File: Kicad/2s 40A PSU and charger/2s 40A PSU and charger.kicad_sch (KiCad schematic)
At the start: 5 parts

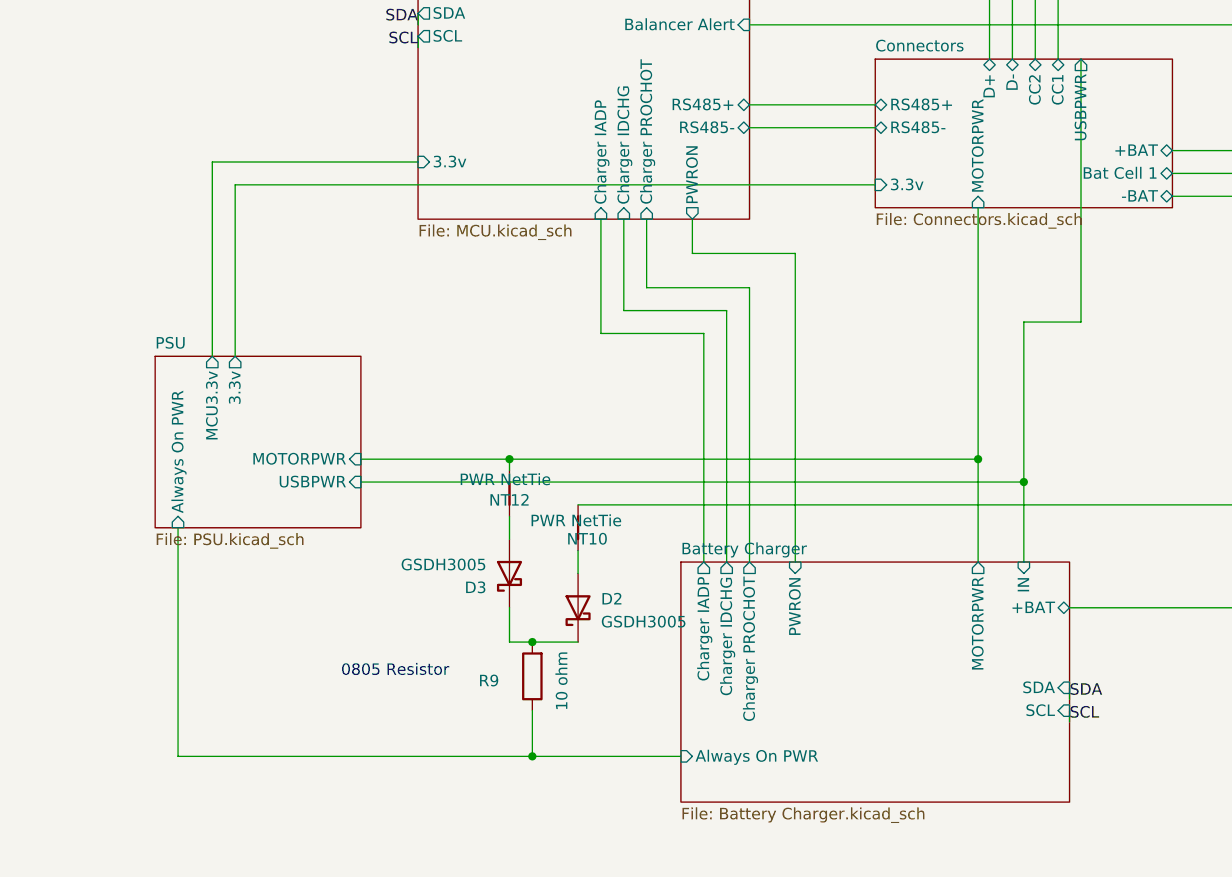
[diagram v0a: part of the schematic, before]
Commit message: Disconnect REGN from unneeded output pullups
These pullups will instead be pulled to 3v3, which should be closer locally. I don't use them but pullups are required for internal detection.
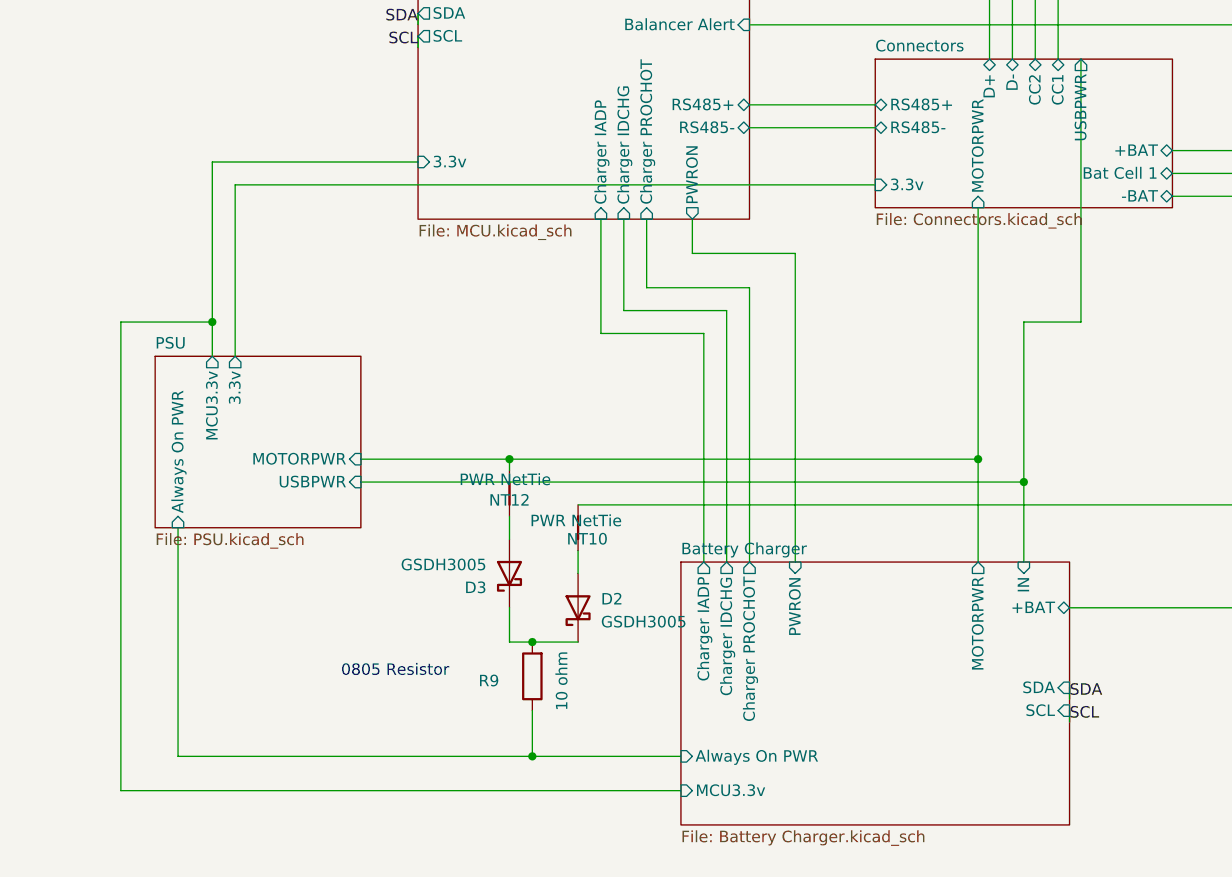
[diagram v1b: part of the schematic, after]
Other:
- sheet Battery Charger ports: added MCU3.3v; removed none
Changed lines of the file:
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@@
+	)
+	(junction
+		(at 74.93 99.06)
+		(diameter 0)
+		(color 0 0 0 0)
 	)
 	(junction
@@
 	(wire
 		(pts
+			(xy 64.77 99.06) (xy 74.93 99.06)
+		)
+		(stroke
+			(width 0)
+			(type default)
+		)
+	)
+	(wire
+		(pts
 			(xy 163.83 59.69) (xy 134.62 59.69)
 		)
@@
 	(wire
 		(pts
+			(xy 74.93 99.06) (xy 74.93 81.28)
+		)
+		(stroke
+			(width 0)
+			(type default)
+		)
+	)
+	(wire
+		(pts
 			(xy 166.37 69.85) (xy 166.37 57.15)
 		)
@@
 	(wire
 		(pts
-			(xy 74.93 102.87) (xy 74.93 81.28)
+			(xy 74.93 102.87) (xy 74.93 99.06)
 		)
 		(stroke
@@
 	(wire
 		(pts
+			(xy 127 151.13) (xy 64.77 151.13)
+		)
+		(stroke
+			(width 0)
+			(type default)
+		)
+	)
+	(wire
+		(pts
 			(xy 110.49 142.24) (xy 110.49 147.32)
 		)
@@
 		(pts
 			(xy 115.57 127) (xy 115.57 124.46)
+		)
+		(stroke
+			(width 0)
+			(type default)
+		)
+	)
+	(wire
+		(pts
+			(xy 64.77 151.13) (xy 64.77 99.06)
 		)
 		(stroke
@@
 	(sheet
 		(at 127 125.73)
-		(size 43.18 26.67)
+		(size 43.18 29.21)
 		(fields_autoplaced yes)
 		(stroke
@@
 		)
 		(property "Sheetfile" "Battery Charger.kicad_sch"
-			(at 127 152.9846 0)
+			(at 127 155.5246 0)
 			(effects
 				(font
@@
 			(effects
 				(font
+					(size 1.27 1.27)
+				)
+				(justify left)
+			)
+		)
+		(pin "MCU3.3v" input
+			(at 127 151.13 180)
+			(effects
+				(font

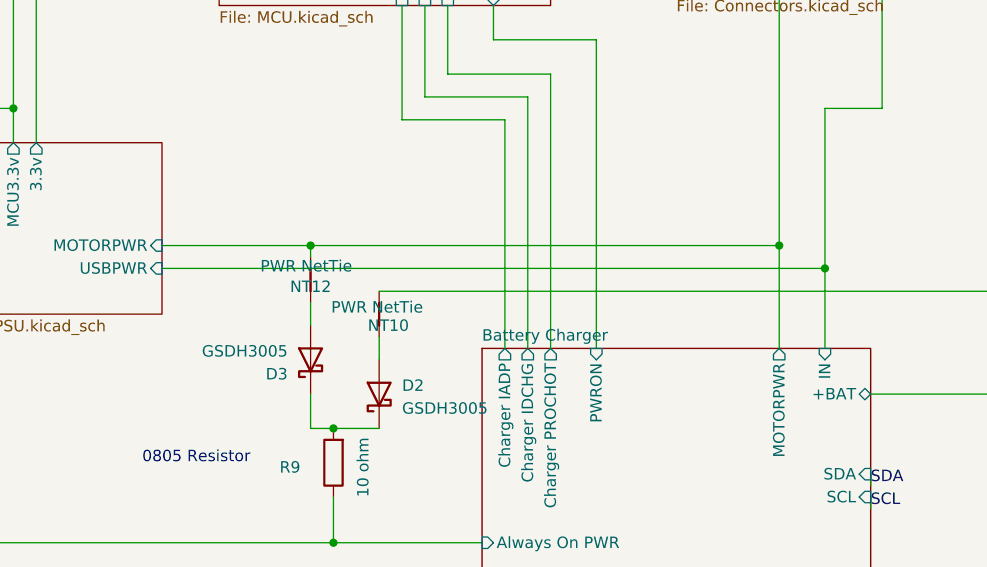
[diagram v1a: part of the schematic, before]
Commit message: Fixed Always On PWR connection
I had it connected to motor power and battery power, what it should have been connected to was USB-C and battery, no barriers whatsoever
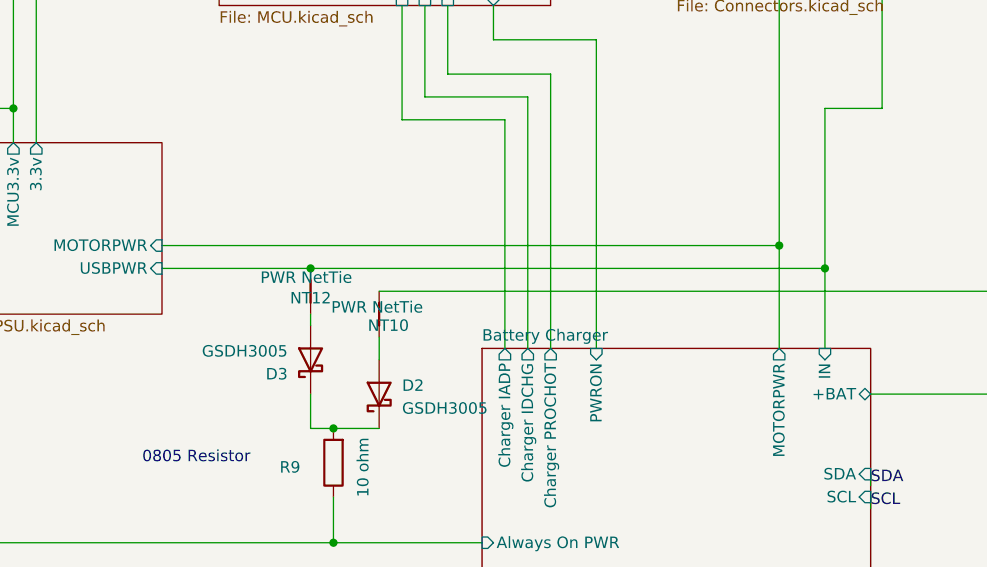
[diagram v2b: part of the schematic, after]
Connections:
- net Battery Charger/IN: now also NT12.2
- net Battery Charger/MOTORPWR: no longer NT12.2
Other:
- moved on the sheet: NT12
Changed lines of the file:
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@@
-	)
-	(junction
-		(at 107.95 114.3)
-		(diameter 0)
-		(color 0 0 0 0)
 	)
 	(junction
@@
 	)
 	(junction
+		(at 107.95 116.84)
+		(diameter 0)
+		(color 0 0 0 0)
+	)
+	(junction
 		(at 189.23 80.01)
 		(diameter 0)
@@
 	(wire
 		(pts
-			(xy 107.95 123.19) (xy 107.95 120.65)
+			(xy 107.95 123.19) (xy 107.95 121.92)
 		)
 		(stroke
@@
 	(wire
 		(pts
-			(xy 91.44 116.84) (xy 165.1 116.84)
+			(xy 91.44 116.84) (xy 107.95 116.84)
 		)
 		(stroke
@@
 	(wire
 		(pts
-			(xy 107.95 114.3) (xy 107.95 115.57)
-		)
-		(stroke
-			(width 0)
-			(type default)
-		)
-	)
-	(wire
-		(pts
 			(xy 139.7 91.44) (xy 139.7 125.73)
 		)
@@
 	(wire
 		(pts
-			(xy 91.44 114.3) (xy 107.95 114.3)
+			(xy 91.44 114.3) (xy 160.02 114.3)
 		)
 		(stroke
@@
 	(wire
 		(pts
-			(xy 107.95 114.3) (xy 160.02 114.3)
-		)
-		(stroke
-			(width 0)
-			(type default)
-		)
-	)
-	(wire
-		(pts
 			(xy 165.1 116.84) (xy 165.1 125.73)
 		)
@@
 		(pts
 			(xy 132.08 97.79) (xy 132.08 125.73)
+		)
+		(stroke
+			(width 0)
+			(type default)
+		)
+	)
+	(wire
+		(pts
+			(xy 107.95 116.84) (xy 165.1 116.84)
 		)
 		(stroke
@@
 	(symbol
 		(lib_id "Device:NetTie_2")
-		(at 107.95 118.11 90)
+		(at 107.95 119.38 90)
 		(unit 1)
 		(exclude_from_sim no)
@@
 		(dnp no)
 		(property "Reference" "NT12"
-			(at 105.664 118.872 90)
+			(at 105.664 120.142 90)
 			(effects
 				(font
@@
 		)
 		(property "Value" "PWR NetTie"
-			(at 102.362 116.586 90)
+			(at 102.362 117.856 90)
 			(effects
 				(font
@@
 		)
 		(property "Footprint" "custom_Connector:NetTie-2_SMD_Pad0.28mm"
-			(at 107.95 118.11 0)
+			(at 107.95 119.38 0)
 			(effects
 				(font
@@
 		)
 		(property "Datasheet" "~"
-			(at 107.95 118.11 0)
+			(at 107.95 119.38 0)
 			(effects
 				(font
@@
 		)
 		(property "Description" "Net tie, 2 pins"
-			(at 107.95 118.11 0)
-			(effects
-				(font
+			(at 107.95 119.38 0)
+			(effects
+				(font
